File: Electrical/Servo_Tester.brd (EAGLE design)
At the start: 20.3 x 63.4 mm, 10 parts, among them IC1 NE555_DIP

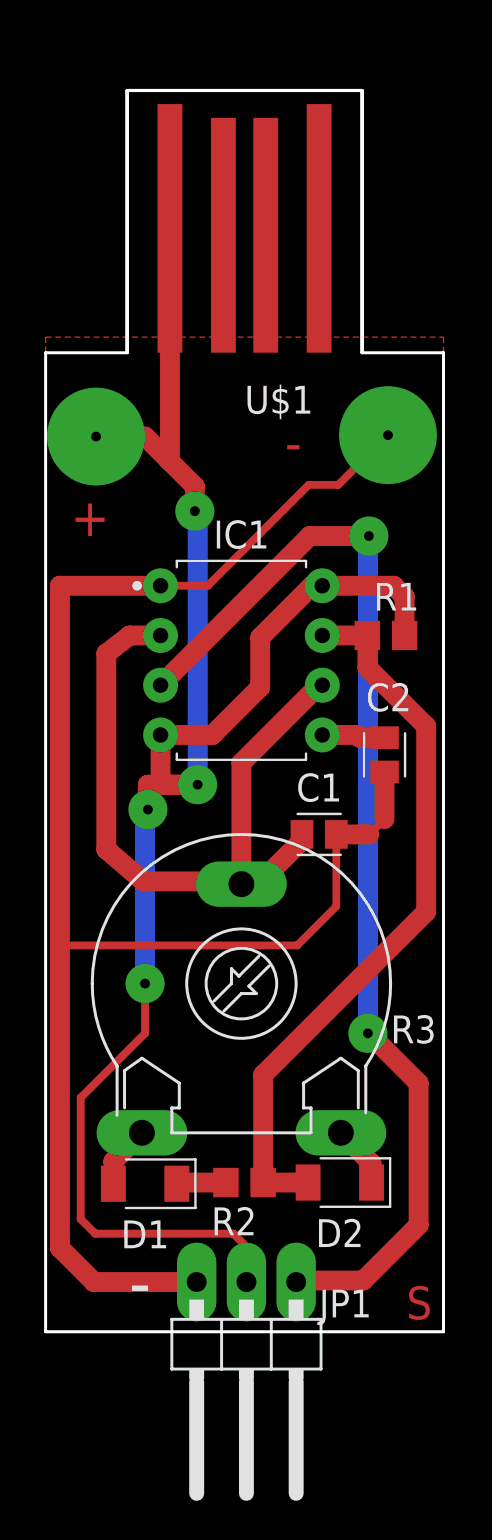
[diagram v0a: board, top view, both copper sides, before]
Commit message: Added LED to PCB, slightly adapted some texts
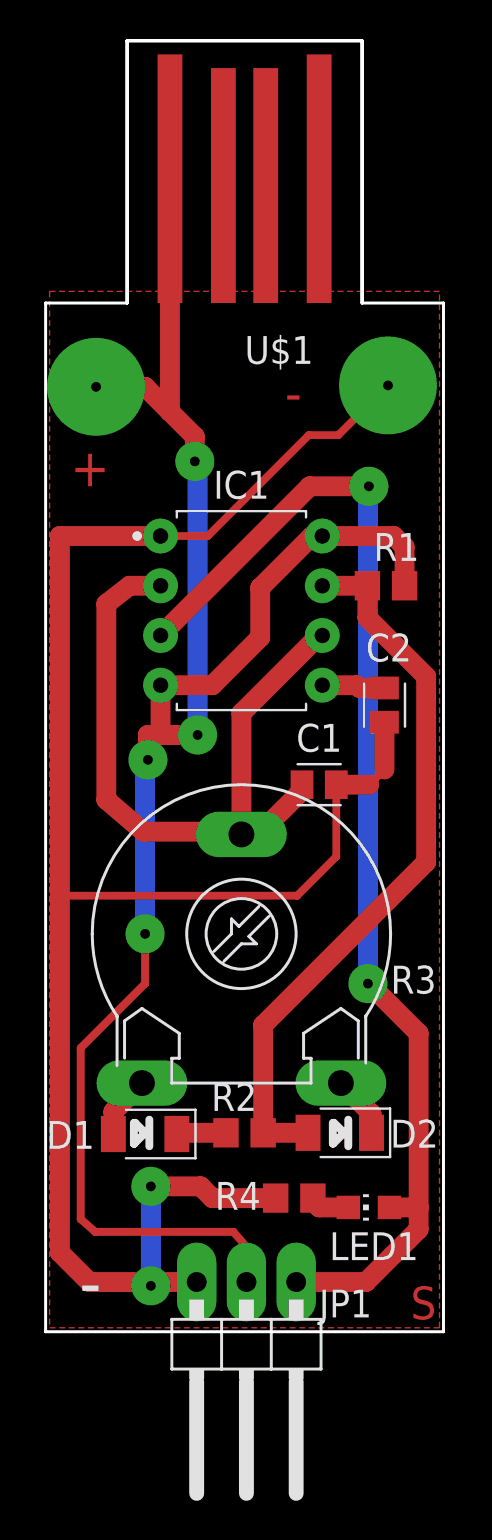
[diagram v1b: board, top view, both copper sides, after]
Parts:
- added LED1: (no value), OwnDevices:CHIP-LED0805
- added R4: 150, OwnDevices:R0805
- moved C1 2.54 mm to (14.0, 27.9)
- moved C2 2.54 mm to (17.3, 32.0)
- moved D2 2.54 mm to (15.0, 10.2)
- moved R2 2.54 mm to (10.2, 10.2)
- moved D1 2.54 mm to (5.08, 10.1)
- moved IC1 2.54 mm to (10.0, 36.8)
- moved R1 2.54 mm to (17.4, 38.1)
- moved R3 2.54 mm to (10.0, 20.3)
- moved U$1 2.54 mm to (10.2, 65.9)
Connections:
- new net N$7: LED1.C, R4.2
- net GND: now also R4.1
- net SERVO: now also LED1.A
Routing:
- net GND: track 85.3 -> 99.7 mm, vias 1 -> 3
- net SERVO: track 57.7 -> 61.8 mm
- net VCC: track 94.1 -> 96.6 mm
- net N$7: track 0.00 -> 2.10 mm
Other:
- board size 20.3 x 63.4 mm -> 20.3 x 65.9 mm
